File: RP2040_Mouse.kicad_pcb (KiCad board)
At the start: 2 copper layers, 54.6 x 30.8 mm, 35 parts, among them J1 DB9_Male, J2 Barrel_Jack_Switch, J3 USB_A, Q1 Q_NPN_BEC, SW1 SW_DPDT_x2, U1 LSF0108PWR, U2 RP2040, U3 AT25SF081B-SSHD-T, U4 AMS1117-3.3, Y1 12MHZ

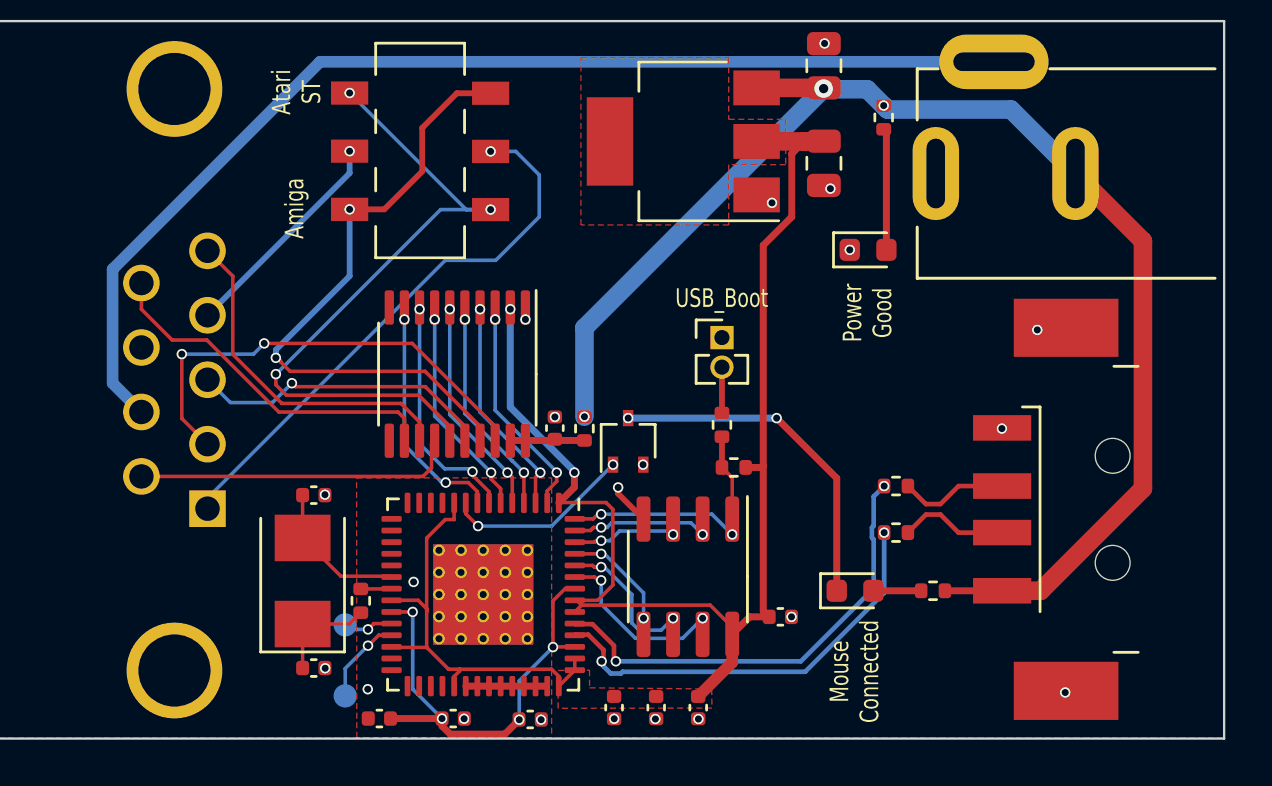
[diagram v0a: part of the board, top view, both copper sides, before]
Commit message: Added pullup resistors on mouse buttons, added breakout points for user software updates
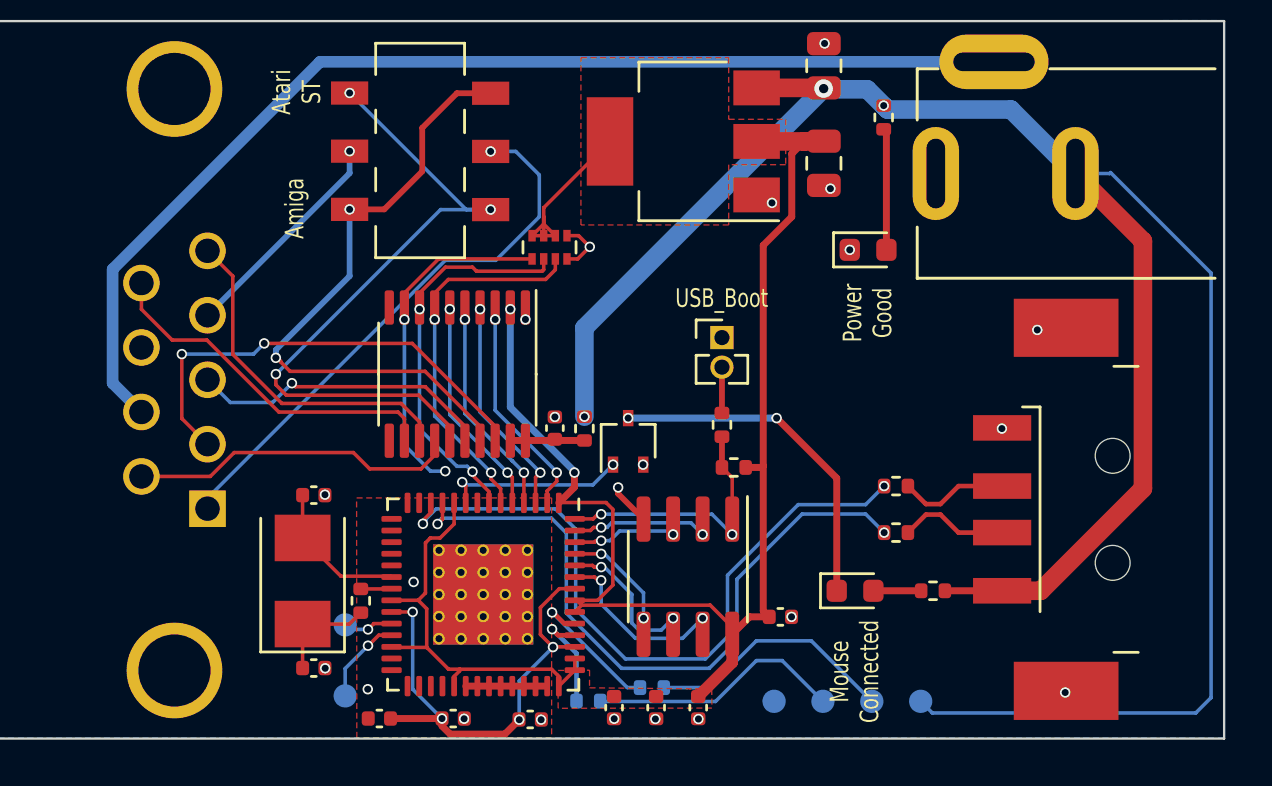
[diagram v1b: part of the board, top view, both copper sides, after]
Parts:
- added R10: 22R, Resistor_SMD:R_0402_1005Metric, B.Cu at (94.5, 86.6)
- added R9: 22R, Resistor_SMD:R_0402_1005Metric, B.Cu at (97.2, 86.0)
- added RN1: R_Pack04, Resistor_SMD:R_Array_Concave_4x0402, F.Cu at (92.8, 67.1)
- added TP3: USB_D+, TestPoint:TestPoint_Pad_D1.0mm, B.Cu at (106.7, 86.6)
- added TP4: USB_D-, TestPoint:TestPoint_Pad_D1.0mm, B.Cu at (104.6, 86.6)
- added TP5: 5v, TestPoint:TestPoint_Pad_D1.0mm, B.Cu at (108.8, 86.6)
- added TP6: GND, TestPoint:TestPoint_Pad_D1.0mm, B.Cu at (102.5, 86.6)
- R1: value 10k -> 10K
- R2: value 200k -> 180K
- R3, R8: value 1k -> 1K5
- R6, R7: value 180R -> 1K5
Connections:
- U2 pad 11: GND -> /USB_T_D-
- U2 pad 12: GND -> /USB_T_D+
- U2 pad 46: /USB_T_D- -> Net-(U2-Pad46)
- U2 pad 47: /USB_T_D+ -> Net-(U2-Pad47)
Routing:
- net +5V: track 58.6 -> 97.5 mm
- net /USB_T_D-: track 18.5 -> 29.6 mm
- net Net-(R10-Pad1): track 0.00 -> 11.0 mm
- net Net-(R9-Pad2): track 0.00 -> 10.8 mm
- net /USB_T_D+: track 19.8 -> 30.5 mm
- net +3V3: track 74.6 -> 82.2 mm
- net ML: track 9.06 -> 15.7 mm
- net MM: track 10.2 -> 16.8 mm
- net Net-(U2-Pad47): track 0.00 -> 6.33 mm, vias 0 -> 1
- net Net-(U2-Pad46): track 0.00 -> 4.65 mm, vias 0 -> 1
- net MR: track 9.82 -> 14.3 mm
- net GND: track 5.29 -> 7.66 mm, vias 21 -> 22
- net +1V1: track 20.1 -> 20.7 mm
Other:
- board text added: "27Ω Resistors for Upgrade"
- board text added: "RP2040 USB To Quadrature Mouse Adapter © 2023 Darrens Lab Rev ${REVISION} - ${ISSUE_DATE}"
- board text added: "USB Firmware Upgrade"
- board text removed: "RP2040 USB To Quadrature Mouse Adapter © 2023 Darrens Lab Rev ${REVISION} - 04.01.2023"

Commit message: Update
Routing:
- net MR: track 14.3 -> 16.5 mm
- net Mouse_Connected: track 7.86 -> 9.07 mm
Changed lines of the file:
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@@
   (segment (start 74.0759 72.9185) (end 74.0759 68.0241) (width 0.5) (layer "B.Cu") (net 11))
   (segment (start 86.615 69.6675) (end 86.615 69.046841) (width 0.154) (layer "F.Cu") (net 12))
+  (segment (start 89.75 78.0625) (end 89.75 77.644242) (width 0.154) (layer "F.Cu") (net 12))
   (segment (start 86.615 69.046841) (end 88.081841 67.58) (width 0.154) (layer "F.Cu") (net 12))
   (segment (start 88.081841 67.58) (end 92.1 67.58) (width 0.154) (layer "F.Cu") (net 12))
+  (segment (start 88.803758 76.698) (end 88.37 76.698) (width 0.154) (layer "F.Cu") (net 12))
+  (segment (start 89.75 77.644242) (end 88.803758 76.698) (width 0.154) (layer "F.Cu") (net 12))
   (via (at 86.615 70.18) (size 0.45) (drill 0.3) (layers "F.Cu" "B.Cu") (net 12))
   (via (at 88.37 76.7) (size 0.45) (drill 0.3) (layers "F.Cu" "B.Cu") (free) (net 12))
@@
   (segment (start 88.37 76.7) (end 87.740064 76.7) (width 0.154) (layer "B.Cu") (net 12))
   (segment (start 86.615 70.18) (end 86.615 75.574936) (width 0.154) (layer "B.Cu") (net 12))
-  (segment (start 89.25 78.0625) (end 89.25 77.32) (width 0.154) (layer "F.Cu") (net 13))
-  (segment (start 89.25 77.32) (end 89.1 77.17) (width 0.154) (layer "F.Cu") (net 13))
-  (segment (start 89.26 78.0725) (end 89.25 78.0625) (width 0.154) (layer "F.Cu") (net 13))
+  (segment (start 89.25 78.0625) (end 89.25 77.644874) (width 0.154) (layer "F.Cu") (net 13))
+  (segment (start 89.25 77.644874) (end 88.807126 77.202) (width 0.154) (layer "F.Cu") (net 13))
+  (segment (start 88.807126 77.202) (end 88.38 77.202) (width 0.154) (layer "F.Cu") (net 13))
   (via (at 95.58 76.42) (size 0.45) (drill 0.3) (layers "F.Cu" "B.Cu") (net 13))
-  (via (at 89.1 77.17) (size 0.45) (drill 0.3) (layers "F.Cu" "B.Cu") (free) (net 13))
+  (via (at 88.38 77.2) (size 0.45) (drill 0.3) (layers "F.Cu" "B.Cu") (free) (net 13))
   (segment (start 95.58 76.42) (end 94.71 77.29) (width 0.154) (layer "B.Cu") (net 13))
+  (segment (start 89.132 77.202) (end 88.38 77.202) (width 0.154) (layer "B.Cu") (net 13))
   (segment (start 94.71 77.29) (end 89.22 77.29) (width 0.154) (layer "B.Cu") (net 13))
-  (segment (start 89.22 77.29) (end 89.1 77.17) (width 0.154) (layer "B.Cu") (net 13))
+  (segment (start 89.22 77.29) (end 89.132 77.202) (width 0.154) (layer "B.Cu") (net 13))
   (segment (start 100.7 79.42) (end 100.7 76.98) (width 0.154) (layer "F.Cu") (net 14))
   (segment (start 93.9375 78.75) (end 94.728064 78.75) (width 0.154) (layer "F.Cu") (net 14))
@@
   (segment (start 102.61 74.42) (end 96.23 74.42) (width 0.3) (layer "B.Cu") (net 43))
   (segment (start 106.7675 81.84) (end 108.82 81.84) (width 0.3) (layer "F.Cu") (net 44))
-  (segment (start 93.9375 83.25) (end 93.962499 83.274999) (width 0.2) (layer "F.Cu") (net 45))
   (segment (start 93.007348 82.77) (end 92.96 82.77) (width 0.2) (layer "F.Cu") (net 45))
   (segment (start 93.487348 83.25) (end 93.007348 82.77) (width 0.2) (layer "F.Cu") (net 45))
@@
   (segment (start 93.22 83.75) (end 92.96 83.49) (width 0.2) (layer "F.Cu") (net 48))
   (segment (start 93.9375 83.75) (end 93.22 83.75) (width 0.2) (layer "F.Cu") (net 48))
-  (segment (start 93.9375 83.75) (end 93.962499 83.725001) (width 0.2) (layer "F.Cu") (net 48))
   (via (at 92.96 83.49) (size 0.45) (drill 0.3) (layers "F.Cu" "B.Cu") (free) (net 48))
   (segment (start 94.01 84.527537) (end 94.01 86.58) (width 0.2) (layer "B.Cu") (net 48))

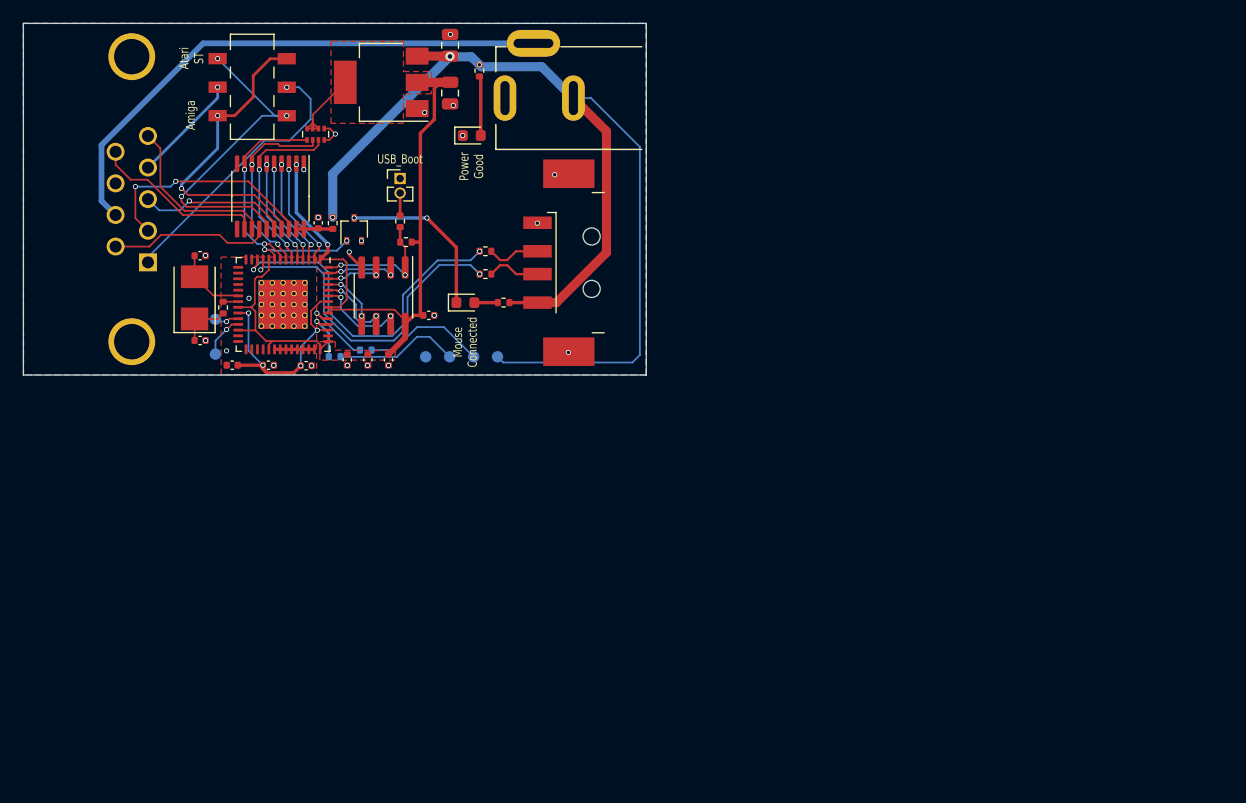
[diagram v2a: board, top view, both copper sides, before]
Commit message: Rev 4, swap the USB pins around to match the requirements of Tinyusb. Add PDF scematic Update 3d renders
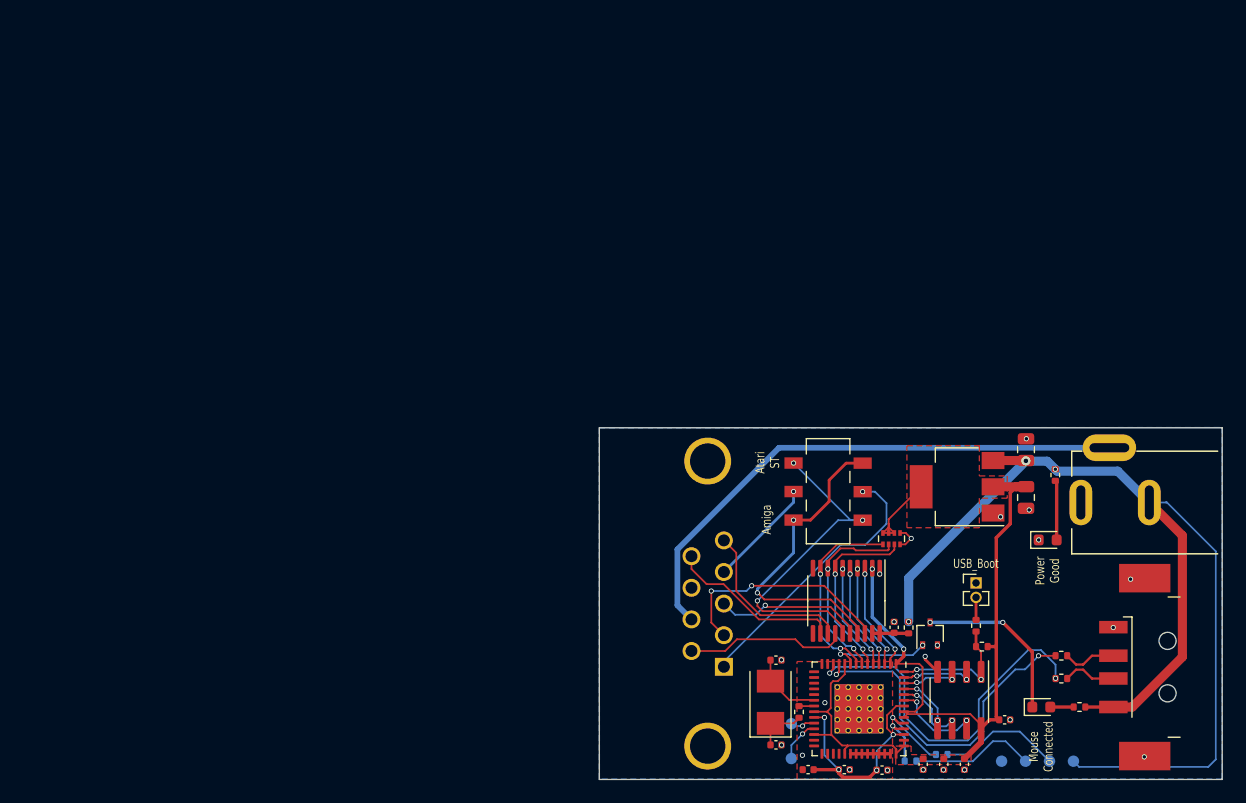
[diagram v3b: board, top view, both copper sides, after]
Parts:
- moved C12 61.7 mm to (149.7, 122.3)
- moved C4 61.7 mm to (153.3, 118.4)
- moved C8 61.7 mm to (139.2, 122.8)
- moved C9 61.7 mm to (142.5, 122.8)
- moved R1 61.7 mm to (151.3, 112.0)
- moved R10 61.7 mm to (145.0, 122.0)
- moved R3 61.7 mm to (135.2, 117.7)
- moved R4 61.7 mm to (158.2, 112.8)
- moved R5 61.7 mm to (158.2, 114.8)
- moved R6 61.7 mm to (157.7, 97.0)
- moved Y1 61.7 mm to (132.7, 116.9)
- moved TP1 61.7 mm to (134.6, 121.8)
- moved C3 61.7 mm to (143.6, 110.3)
- moved JP1 61.7 mm to (150.7, 106.4)
- moved R8 61.7 mm to (150.7, 110.2)
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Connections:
- U2 pad 11: /USB_T_D- -> /USB_T_D+
- U2 pad 12: /USB_T_D+ -> /USB_T_D-
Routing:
- net /USB_T_D-: track 29.6 -> 32.0 mm
- net /USB_T_D+: track 30.5 -> 29.8 mm

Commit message: Merging local branches
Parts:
- added G***: LOGO, My Libs:dl_logo_small, B.Cu at (160.9, 109.4)
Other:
- board text added: "RP2040 USB To Quadrature Mouse Adapter Rev ${REVISION} - ${ISSUE_DATE}"
- board text added: "© 2023"
- board text removed: "RP2040 USB To Quadrature Mouse Adapter © 2023 Darrens Lab Rev ${REVISION} - ${ISSUE_DATE}"

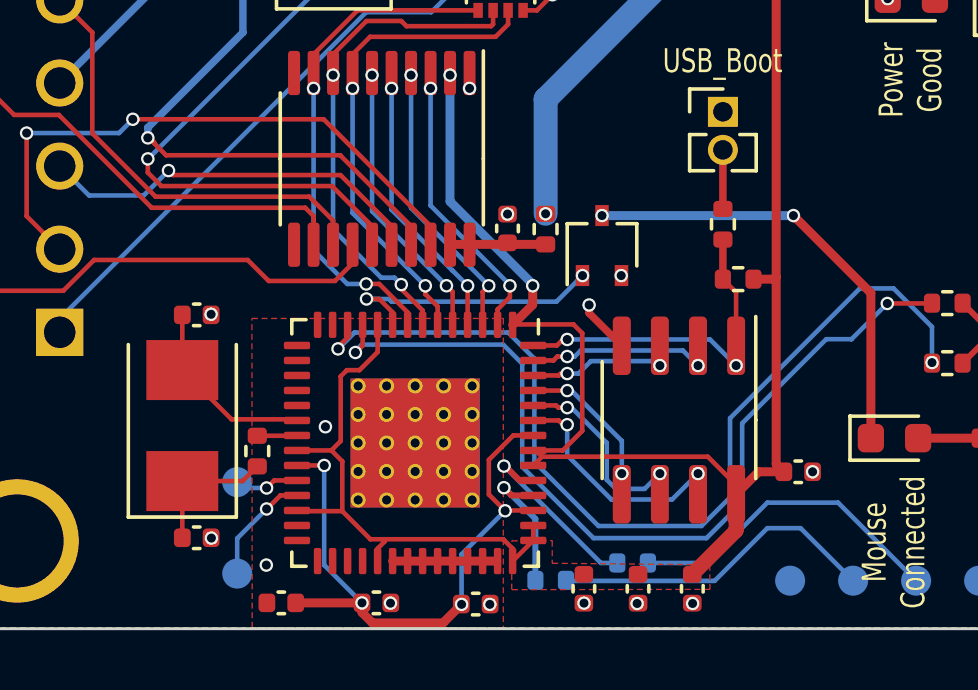
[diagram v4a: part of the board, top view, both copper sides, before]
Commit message: Fix footprint issue from 2nd PCB run, pannelize for prod, new pics, new label
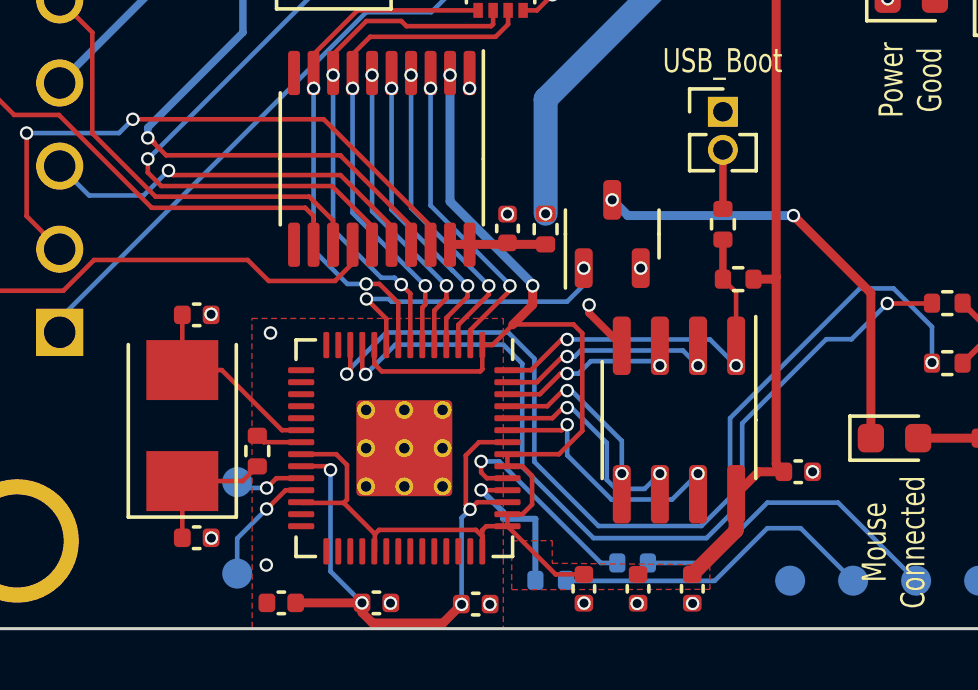
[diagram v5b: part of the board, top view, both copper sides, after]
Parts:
- Q1: footprint Package_TO_SOT_SMD:SOT-323_SC-70 -> Package_TO_SOT_SMD:SOT-23-3
- U2: footprint Package_DFN_QFN:QFN-56-1EP_8x8mm_P0.5mm_EP4.3x4.3mm_ThermalVias -> Library:RP2040-QFN-56
- moved Q1 0.51 mm to (147.1, 110.5)
- moved U2 0.40 mm to (140.1, 117.6)
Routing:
- net GND: track 7.66 -> 4.19 mm
- net QSPI_SS: track 11.6 -> 12.8 mm
- net QSPI_SD1: track 5.84 -> 7.00 mm
- net QSPI_SD2: track 4.48 -> 5.60 mm
- net QSPI_SD0: track 4.74 -> 5.81 mm
- net XA: track 9.15 -> 10.2 mm
- net XB: track 9.48 -> 10.5 mm
- net QSPI_CLK: track 6.31 -> 7.28 mm
- net Net-(R9-Pad1): track 6.29 -> 7.27 mm
- net YA: track 8.94 -> 9.90 mm
- net QSPI_SD3: track 7.54 -> 8.42 mm
- net Mouse_Connected: track 9.07 -> 9.88 mm
- net YB: track 9.43 -> 10.2 mm
- net Net-(R10-Pad2): track 4.62 -> 5.28 mm
- net MR: track 16.5 -> 17.1 mm
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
